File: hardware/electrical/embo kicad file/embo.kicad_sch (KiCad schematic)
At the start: 105 parts, among them IC1 OPA2354, IC2 OPA2354, J1 Conn_Coaxial, J13 USB_C_Receptacle_USB2.0_16P, J14 24 V PSU input, J2 Conn_Coaxial, J3 UART to RPi, J4 JSTXH 6pin Socket 1, J5 JSTXH 6pin Socket 2, J6 motor 1, J7 motor 2, J8 LED Panel, J9 Conn_02x10_Odd_Even, Q1 AO4407A, U1 ESP32-S3-WROOM-1, U2 LM2596S-5, U3 AMS1117-3.3, U4 AD9833xRM, U5 TMC2209-LA, U6 TMC2209-LA

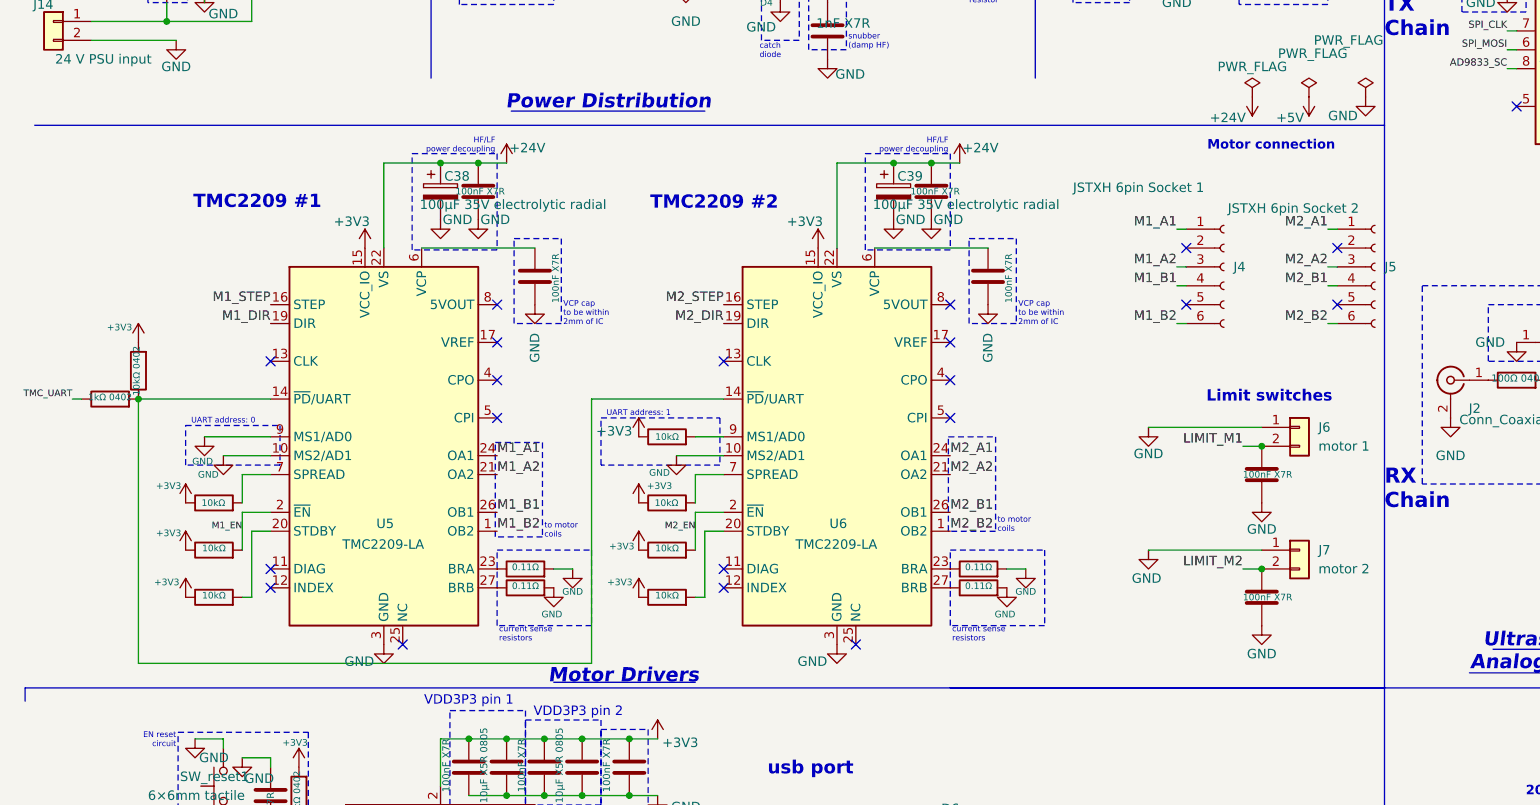
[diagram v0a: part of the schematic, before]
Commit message: main PCB layout update
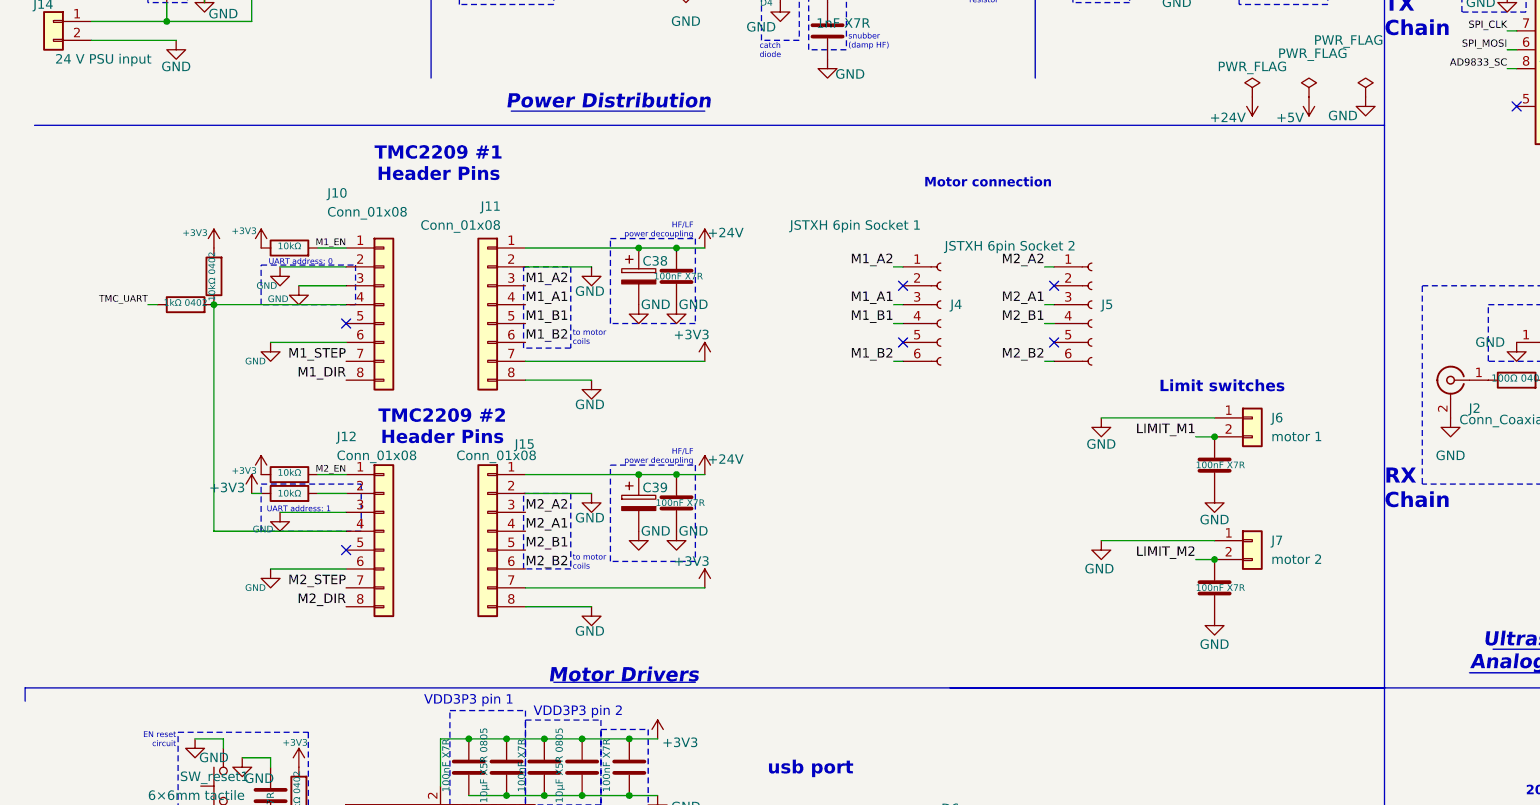
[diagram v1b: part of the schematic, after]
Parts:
- removed C15, C37: 100nF X7R, Capacitor_SMD:C_0402_1005Metric_Pad0.74x0.62mm_HandSolder, symbol Device:C
- removed R13, R2, R3, R4: 10kΩ, Resistor_SMD:R_0402_1005Metric_Pad0.72x0.64mm_HandSolder, symbol Device:R
- removed R15, R16, R7, R8: 0.11Ω, Resistor_SMD:R_2512_6332Metric, symbol Device:R
- removed U5, U6: TMC2209-LA, Package_DFN_QFN:VQFN-28-1EP_5x5mm_P0.5mm_EP3.7x3.7mm_ThermalVias, symbol Driver_Motor:TMC2209-LA
- added J10, J11, J12, J15: Conn_01x08, Connector_PinSocket_2.54mm:PinSocket_1x08_P2.54mm_Vertical, symbol Connector_Generic:Conn_01x08
- C38, C39: footprint Capacitor_THT:C_Radial_D6.3mm_H11.0mm_P2.50mm -> Capacitor_THT:C_Radial_D6.3mm_H7.0mm_P2.50mm
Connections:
- net +24V: now also J11.1 (Pin_1), J15.1 (Pin_1)
- net +3V3: now also J11.7 (Pin_7), J15.7 (Pin_7)
- net GND: now also J10.2 (Pin_2), J10.3 (Pin_3), J10.6 (Pin_6), J11.2 (Pin_2), J11.8 (Pin_8), J12.3 (Pin_3), J12.6 (Pin_6), J15.2 (Pin_2), J15.8 (Pin_8)
- net M1_A1: now also J4.3 (Pin_3), J11.4 (Pin_4); no longer J4.1 (Pin_1)
- net M1_A2: now also J4.1 (Pin_1), J11.3 (Pin_3); no longer J4.3 (Pin_3)
- net M1_B1: now also J11.5 (Pin_5)
- net M1_B2: now also J11.6 (Pin_6)
- net M1_DIR: now also J10.8 (Pin_8)
- net M1_EN: now also J10.1 (Pin_1)
- net M1_STEP: now also J10.7 (Pin_7)
- net M2_A1: now also J5.3 (Pin_3), J15.4 (Pin_4); no longer J5.1 (Pin_1)
- net M2_A2: now also J5.1 (Pin_1), J15.3 (Pin_3); no longer J5.3 (Pin_3)
- net M2_B1: now also J15.5 (Pin_5)
- net M2_B2: now also J15.6 (Pin_6)
- net M2_DIR: now also J12.8 (Pin_8)
- net M2_EN: now also J12.1 (Pin_1)
- net M2_STEP: now also J12.7 (Pin_7)
- net at R_PDN_UP1.1, R_UART1.2: now also J10.4 (Pin_4), J12.4 (Pin_4)
- net at R12.2: now also J12.2 (Pin_2)
- no-connect marks 29 -> 15
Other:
- note added: "TMC2209 #1 Header Pins"
- note added: "TMC2209 #2 Header Pins"
- note removed: "TMC2209 #1"
- note removed: "TMC2209 #2"
- note removed: "VCP cap to be within 2mm of IC"
- note removed: "current sense resistors"
- moved on the sheet: J4, J5, J6, J7
